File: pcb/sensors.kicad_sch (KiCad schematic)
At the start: 4 parts, among them U2 HDC1080, U3 LTR-303ALS-01

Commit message: Change schematic name
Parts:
- added C10, C11: 0.1uF, Capacitor_SMD:C_0603_1608Metric, symbol Device:C
- added C12, C9: 1uF, Capacitor_SMD:C_0603_1608Metric, symbol Device:C
- added R6: 4R7, Resistor_SMD:R_0603_1608Metric, symbol Device:R_US
- added U8: SGP40-D-R4, CRG Makes:SON80P244X244X95-7N, symbol CRG Makes:SGP40-D-R4
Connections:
- net +3.3V: now also C10.1, C11.1, C9.1, R6.1, U8.5 (VDDH)
- net GND: now also C10.2, C11.2, C12.2, C9.2, U8.2 (VSS), U8.4 (N/A), U8.7 (EP)
- net SCL: now also U8.6 (SCL)
- net SDA: now also U8.3 (SDA)
- new net: C12.1, R6.2, U8.1 (VDD)
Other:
- title: Environment Module -> Client

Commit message: Updated project name and properties
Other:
- title: Client -> Client Hardware
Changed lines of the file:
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@@
 	(paper "A4")
 	(title_block
-		(title "Client")
+		(title "Client Hardware")
 		(date "<<release-date>>")
 		(rev "<<tag>>")

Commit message: Switch cap/res to CRGM footprint
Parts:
- C10, C11, C12, C9: footprint Capacitor_SMD:C_0603_1608Metric -> CRGM Passive:C_0603_1608Metric
- R2, R3, R6: footprint Resistor_SMD:R_0603_1608Metric -> CRGM Passive:R_0603_1608Metric
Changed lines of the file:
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@@
 			)
 		)
-		(property "Footprint" "Resistor_SMD:R_0603_1608Metric"
+		(property "Footprint" "CRGM Passive:R_0603_1608Metric"
 			(at 58.166 101.854 90)
 			(effects
@@
 			)
 		)
-		(property "Footprint" "Capacitor_SMD:C_0603_1608Metric"
+		(property "Footprint" "CRGM Passive:C_0603_1608Metric"
 			(at 101.2952 116.84 0)
 			(effects
@@
 			)
 		)
-		(property "Footprint" "Capacitor_SMD:C_0603_1608Metric"
+		(property "Footprint" "CRGM Passive:C_0603_1608Metric"
 			(at 98.7552 50.8 0)
 			(effects
@@
 			)
 		)
-		(property "Footprint" "Capacitor_SMD:C_0603_1608Metric"
+		(property "Footprint" "CRGM Passive:C_0603_1608Metric"
 			(at 58.1152 115.57 0)
 			(effects
@@
 			)
 		)
-		(property "Footprint" "Resistor_SMD:R_0603_1608Metric"
+		(property "Footprint" "CRGM Passive:R_0603_1608Metric"
 			(at 68.326 27.686 90)
 			(effects
@@
 			)
 		)
-		(property "Footprint" "Resistor_SMD:R_0603_1608Metric"
+		(property "Footprint" "CRGM Passive:R_0603_1608Metric"
 			(at 60.706 27.686 90)
 			(effects
@@
 			)
 		)
-		(property "Footprint" "Capacitor_SMD:C_0603_1608Metric"
+		(property "Footprint" "CRGM Passive:C_0603_1608Metric"
 			(at 101.2952 81.28 0)
 			(effects

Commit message: Added renders and aligned connectors
Added renders
Aligned connectors to grid
Added dimensions
Fixed part numbers and values
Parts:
- U2: MPN (none) -> HDC1080
- U3: MPN (none) -> LTR-303ALS-01
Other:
- title: Client Hardware -> Client
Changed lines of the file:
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@@
 	(paper "A4")
 	(title_block
-		(title "Client Hardware")
+		(title "Client")
 		(date "<<release-date>>")
 		(rev "<<tag>>")
@@
 			)
 		)
+		(property "MPN" "HDC1080"
+			(at 82.55 46.99 0)
+			(effects
+				(font
+					(size 1.27 1.27)
+				)
+				(hide yes)
+			)
+		)
 		(pin "7"
 		)
@@
 			(effects
 				(font
+					(size 1.27 1.27)
+				)
+				(hide yes)
+			)
+		)
+		(property "MPN" "LTR-303ALS-01"
+			(at 82.55 77.47 0)
+			(effects
+				(font

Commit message: Updated descriptions; fixed MN
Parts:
- R2, R3: MN FOJAN -> FOJAN
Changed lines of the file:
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@@
 			)
 		)
-		(property "MN" "FOJAN "
+		(property "MN" "FOJAN"
 			(at 67.31 27.94 0)
 			(effects
@@
 			)
 		)
-		(property "MN" "FOJAN "
+		(property "MN" "FOJAN"
 			(at 59.69 27.94 0)
 			(effects

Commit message: Added RF connector; re-placed and re-routed
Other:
- title: Client -> Aquarius Client
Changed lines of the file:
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@@
 	(paper "A4")
 	(title_block
-		(title "Client")
+		(title "Aquarius Client")
 		(date "<<release-date>>")
 		(rev "<<tag>>")

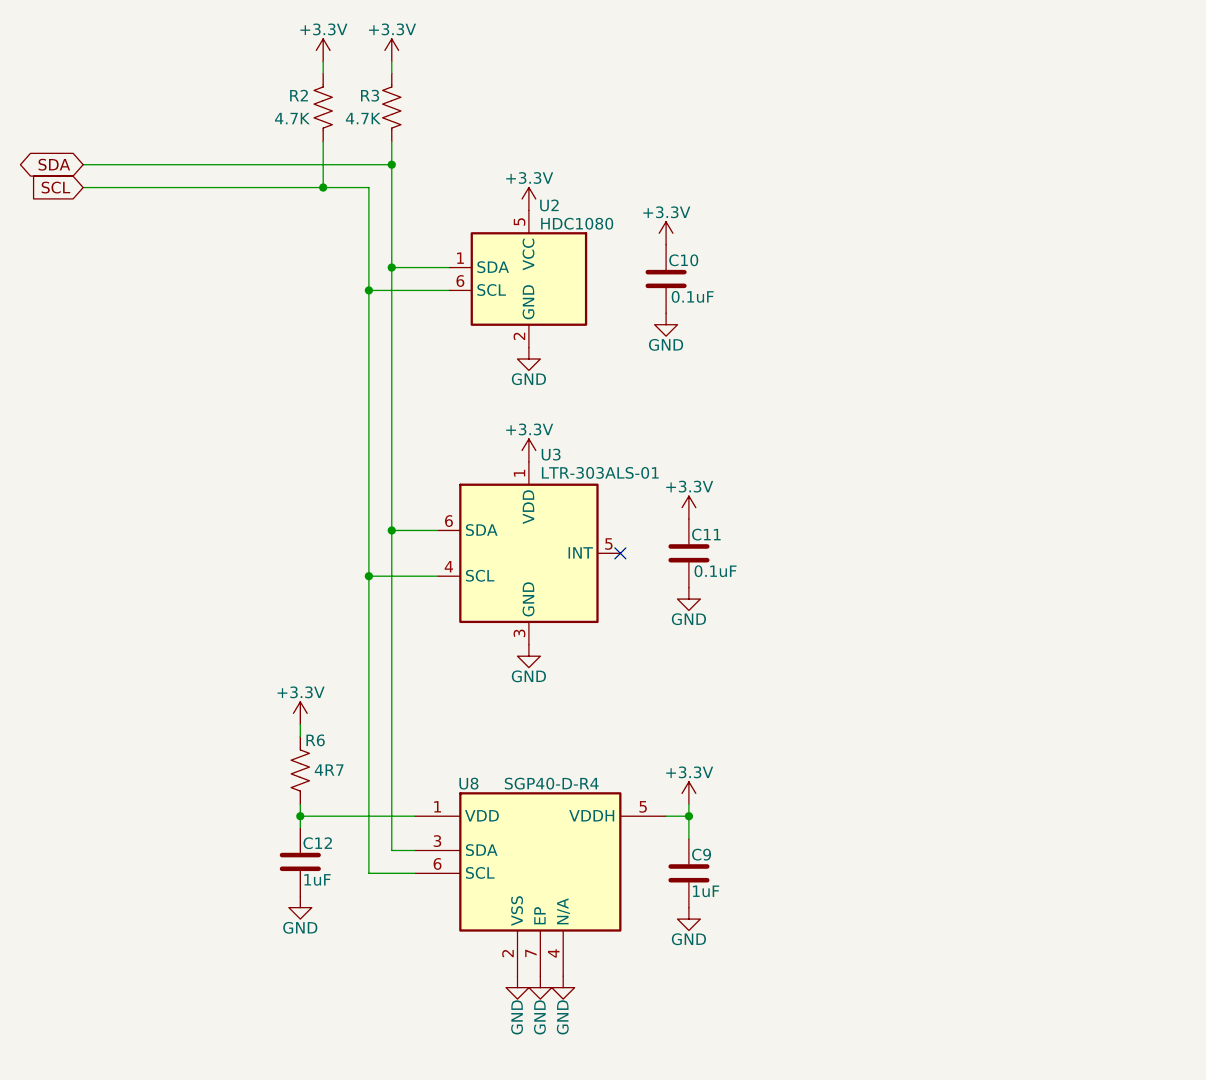
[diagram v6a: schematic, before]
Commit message: Removed indictors sheet
Fixed attribute consistency with schematic and symbols
Moved logos to separate box
Updated DRC warnings/ignore
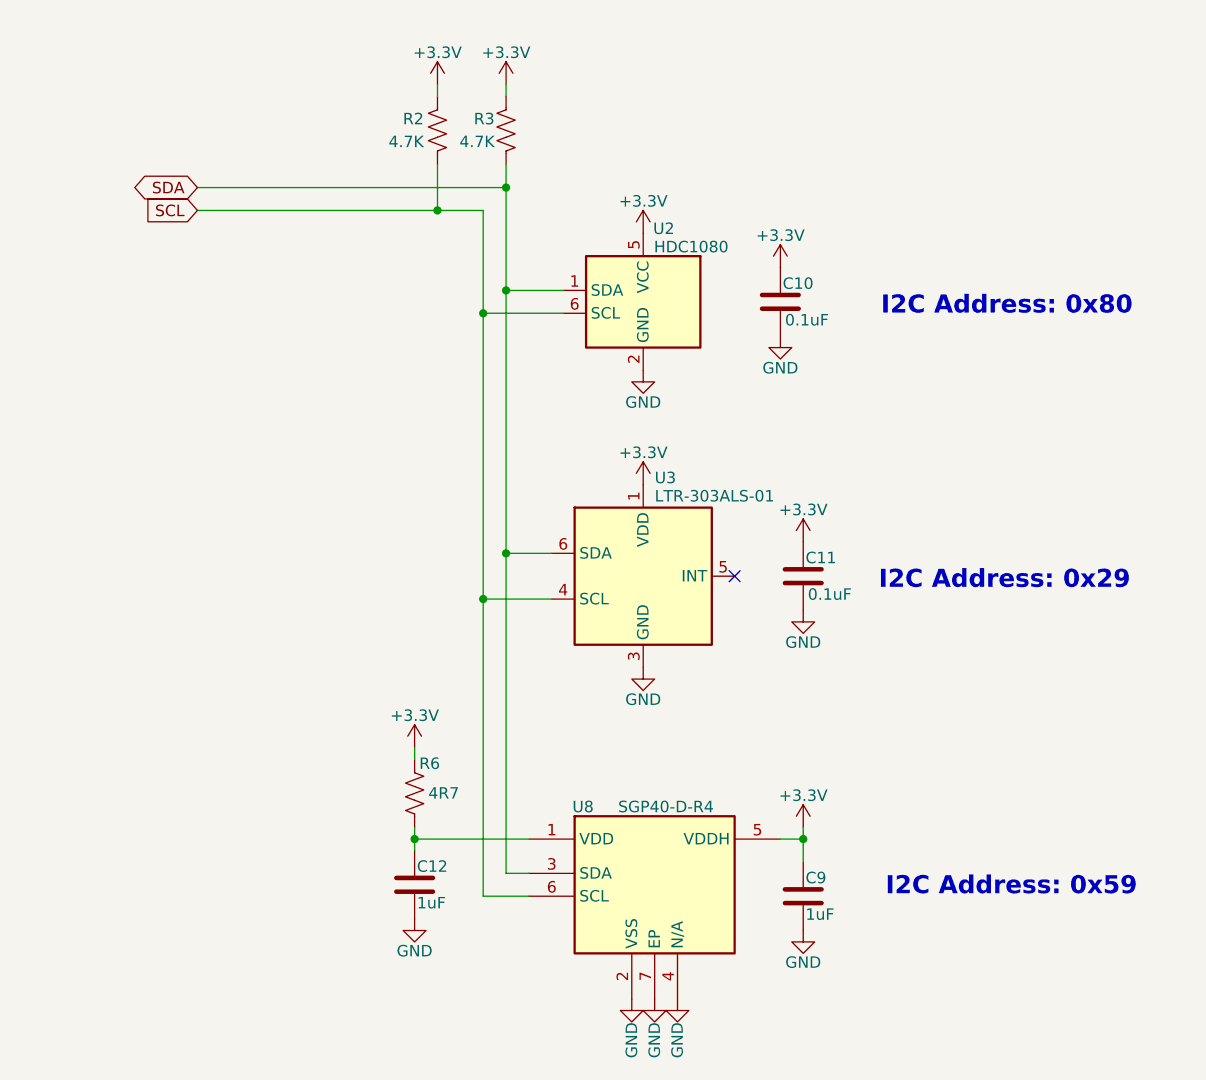
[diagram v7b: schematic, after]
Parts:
- U2: MN (none) -> TI; MPN HDC1080 -> HDC1080DMBR
- U3: MN (none) -> LiteOn
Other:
- note added: "I2C Address: 0x29"
- note added: "I2C Address: 0x59"
- note added: "I2C Address: 0x80"
- moved on the sheet: C10, C11, C12, C9, R2, R3, R6, U2, U3, U8

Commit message: Updated part attributes for consistency
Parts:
- C10, C11: Tolerance (none) -> 10%
- R2, R3: Digikey 541-3993-2-ND -> CR0603-JW-472ELFTR-ND; Mouser 71-CRCW06034K70JNEAC -> 652-CR0603-JW-472ELF; Tolerance (none) -> 5%
- R6: Tolerance (none) -> 5%
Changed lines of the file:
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@@
 			)
 		)
-		(property "Datasheet" "~"
+		(property "Datasheet" "https://bourns.com/docs/product-datasheets/cr.pdf?sfvrsn=574d41f6_14"
 			(at 69.85 104.14 0)
 			(effects
@@
 		)
 		(property "LCSC" "C2907168"
+			(at 69.85 104.14 0)
+			(effects
+				(font
+					(size 1.27 1.27)
+				)
+				(hide yes)
+			)
+		)
+		(property "Tolerance" "5%"
 			(at 69.85 104.14 0)
 			(effects
@@
 			)
 		)
+		(property "Tolerance" "10%"
+			(at 110.49 49.53 0)
+			(effects
+				(font
+					(size 1.27 1.27)
+				)
+				(hide yes)
+			)
+		)
 		(pin "1"
 		)
@@
 			)
 		)
-		(property "Datasheet" "~"
+		(property "Datasheet" "https://bourns.com/docs/product-datasheets/cr.pdf?sfvrsn=574d41f6_14"
 			(at 80.01 30.48 0)
 			(effects
@@
 			)
 		)
-		(property "Description" "Resistor, US symbol"
+		(property "Description" "Thick Film Resistors - SMD 1/10Watt 4.7Kohms 5%"
 			(at 80.01 30.48 0)
 			(effects
@@
 			)
 		)
-		(property "Digikey" "541-3993-2-ND"
+		(property "Digikey" "CR0603-JW-472ELFTR-ND"
 			(at 80.01 30.48 0)
 			(effects
@@
 			)
 		)
-		(property "Mouser" "71-CRCW06034K70JNEAC"
+		(property "Mouser" "652-CR0603-JW-472ELF"
+			(at 80.01 30.48 0)
+			(effects
+				(font
+					(size 1.27 1.27)
+				)
+				(hide yes)
+			)
+		)
+		(property "Tolerance" "5%"
 			(at 80.01 30.48 0)
 			(effects
@@
 			)
 		)
-		(property "Datasheet" "~"
+		(property "Datasheet" "https://bourns.com/docs/product-datasheets/cr.pdf?sfvrsn=574d41f6_14"
 			(at 72.39 30.48 0)
 			(effects
@@
 			)
 		)
-		(property "Description" "Resistor, US symbol"
+		(property "Description" "Thick Film Resistors - SMD 1/10Watt 4.7Kohms 5%"
 			(at 72.39 30.48 0)
 			(effects
@@
 			)
 		)
-		(property "Mouser" "71-CRCW06034K70JNEAC"
+		(property "Mouser" "652-CR0603-JW-472ELF"
 			(at 72.39 30.48 0)
 			(effects
@@
 			)
 		)
-		(property "Digikey" "541-3993-2-ND"
+		(property "Digikey" "CR0603-JW-472ELFTR-ND"
 			(at 72.39 30.48 0)
 			(effects
@@
 			)
 		)
+		(property "Tolerance" "5%"
+			(at 72.39 30.48 0)
+			(effects
+				(font
+					(size 1.27 1.27)
+				)
+				(hide yes)
+			)
+		)
 		(pin "2"
 		)
@@
 			(at 113.03 80.01 0)
 			(effects
+				(font
+					(size 1.27 1.27)
+				)
+				(hide yes)
+			)
+		)
+		(property "Tolerance" "10%"
+			(at 113.03 80.01 0)
+			(effects
